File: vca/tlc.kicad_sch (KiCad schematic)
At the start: 14 parts, among them U5 TL074, U6 TL074, U7 TLC7528

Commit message: some fixes, starting to work on PCB
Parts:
- added R40: R-2k-1206, Resistor_SMD:R_1206_3216Metric_Pad1.30x1.75mm_HandSolder, symbol eurorack:R-2k-1206
- added R41: R-10k-1206, Resistor_SMD:R_1206_3216Metric_Pad1.30x1.75mm_HandSolder, symbol eurorack:R-10k-1206
- gave numbers to parts that had none: 3
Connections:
- net +12V: now also R40.1
- net GND: now also R41.2; no longer U6.5 (+)
- net +10V: now reaches U6.6 (-), U6.7
- new net: R40.2, R41.1, U6.5 (+)
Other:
- moved on the sheet: U6B

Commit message: working on front panel
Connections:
- net +10V renamed B_+10V
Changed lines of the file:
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@@
     (stroke (width 0) (type default) (color 0 0 0 0))
   )
-  (wire (pts (xy 272.415 137.16) (xy 276.225 137.16))
+  (wire (pts (xy 272.415 137.16) (xy 274.32 137.16))
     (stroke (width 0) (type default) (color 0 0 0 0))
   )
@@
   (text "For DAC\n" (at 219.71 27.305 0)
     (effects (font (size 1.27 1.27)) (justify left bottom))
+  )
+  (global_label "B_+10V" (shape output) (at 274.32 137.16 0) (fields_autoplaced)
+    (effects (font (size 1.27 1.27)) (justify left))
+    (property "Intersheet References" "${INTERSHEET_REFS}" (id 0) (at 284.0507 137.0806 0)
+      (effects (font (size 1.27 1.27)) (justify left) hide)
+    )
   )
   (hierarchical_label "CS" (shape input) (at 71.12 102.87 180)
@@
     (pin "2")
   )
-  (symbol (lib_id "power:+10V") (at 276.225 137.16 0) (unit 1)
-    (in_bom yes) (on_board yes) (fields_autoplaced)
-    (property "Reference" "#PWR0181" (id 0) (at 276.225 140.97 0)
-      (effects (font (size 1.27 1.27)) hide)
-    )
-    (property "Value" "+10V" (id 1) (at 276.225 132.08 0))
-    (property "Footprint" "" (id 2) (at 276.225 137.16 0)
-      (effects (font (size 1.27 1.27)) hide)
-    )
-    (property "Datasheet" "" (id 3) (at 276.225 137.16 0)
-      (effects (font (size 1.27 1.27)) hide)
-    )
-    (pin "1")
-  )
   (symbol (lib_id "power:GND") (at 160.655 104.775 0) (unit 1)

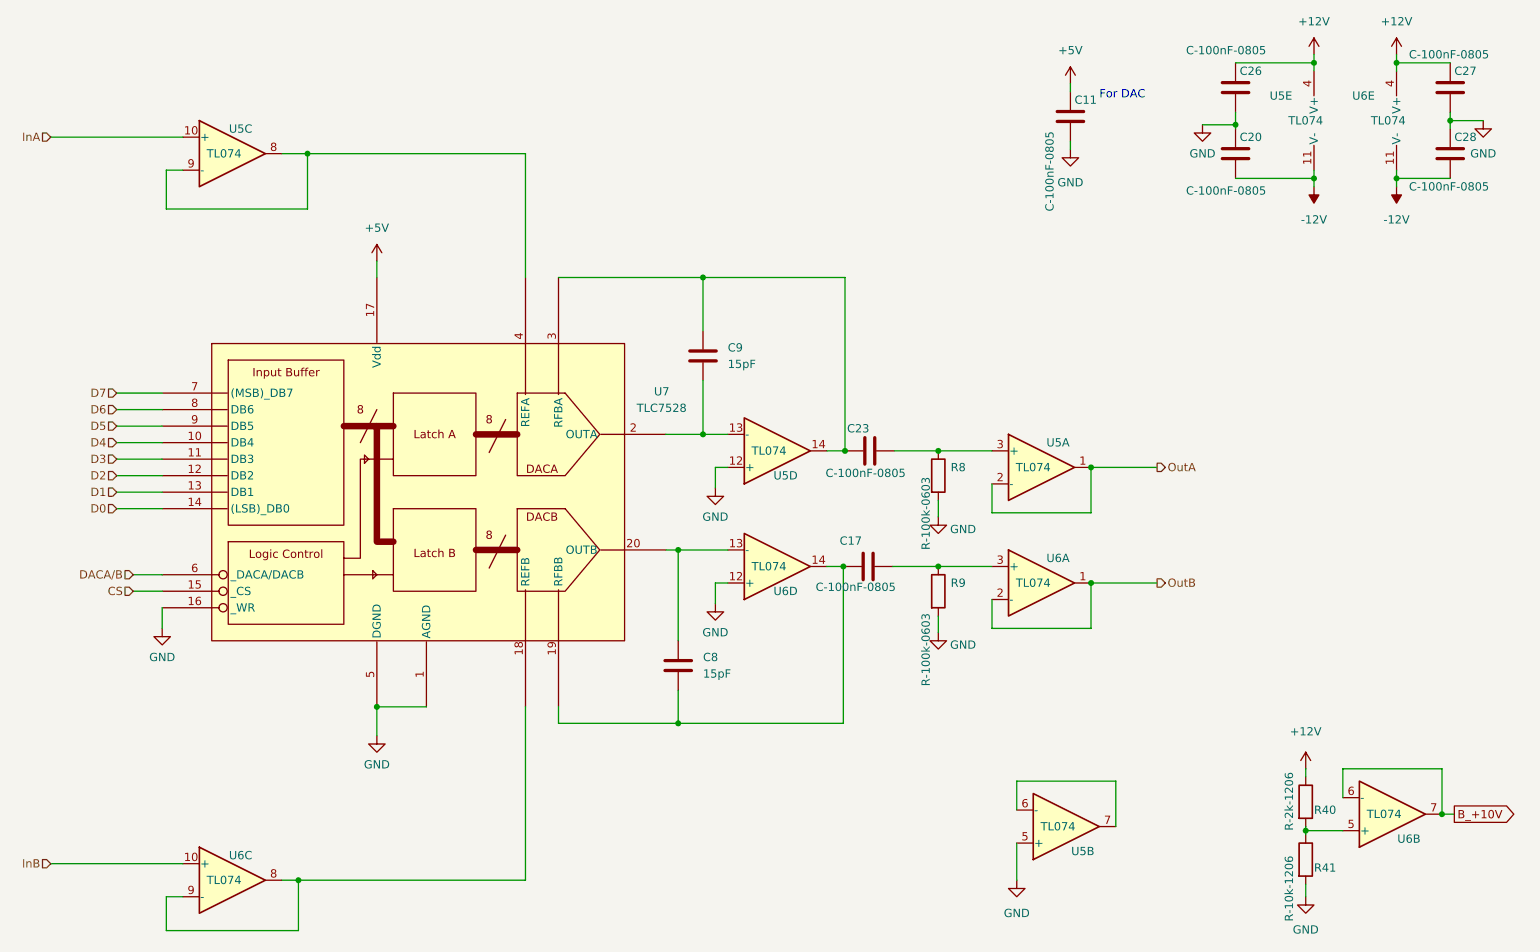
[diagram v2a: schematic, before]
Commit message: fixing drc issues
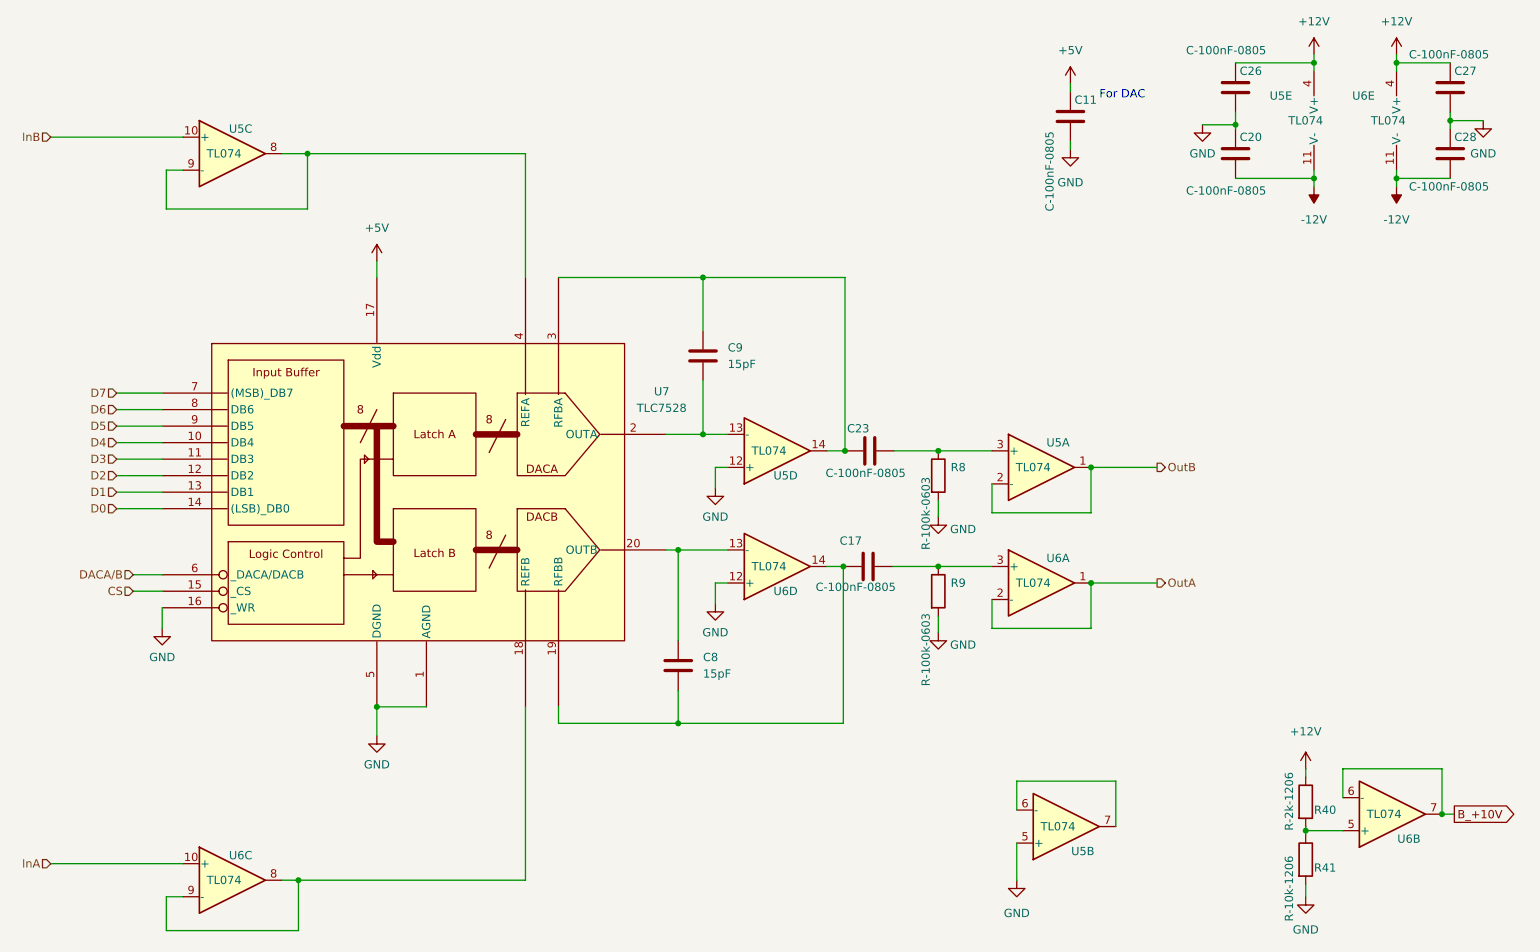
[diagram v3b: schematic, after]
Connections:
- net InA: now also U6.10 (+); no longer U5.10 (+)
- net InB: now also U5.10 (+); no longer U6.10 (+)
- net OutA: now also U6.1, U6.2 (-); no longer U5.1, U5.2 (-)
- net OutB: now also U5.1, U5.2 (-); no longer U6.1, U6.2 (-)
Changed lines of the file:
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@@
     (effects (font (size 1.27 1.27)) (justify right))
   )
-  (hierarchical_label "OutB" (shape output) (at 228.6 101.6 0)
+  (hierarchical_label "OutB" (shape output) (at 228.6 83.82 0)
     (effects (font (size 1.27 1.27)) (justify left))
   )
@@
     (effects (font (size 1.27 1.27)) (justify right))
   )
-  (hierarchical_label "InB" (shape input) (at 58.42 144.78 180)
+  (hierarchical_label "InB" (shape input) (at 58.42 33.02 180)
     (effects (font (size 1.27 1.27)) (justify right))
   )
-  (hierarchical_label "OutA" (shape output) (at 228.6 83.82 0)
+  (hierarchical_label "OutA" (shape output) (at 228.6 101.6 0)
     (effects (font (size 1.27 1.27)) (justify left))
   )
-  (hierarchical_label "InA" (shape input) (at 58.42 33.02 180)
+  (hierarchical_label "InA" (shape input) (at 58.42 144.78 180)
     (effects (font (size 1.27 1.27)) (justify right))
   )
